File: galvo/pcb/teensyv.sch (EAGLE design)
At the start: 53 parts, among them IC1 RB-0512D, IC10 MCP4922-E/P, IC2.5 MAX6102, IC3 QUAD_OPAMPP, IC5 MAX6105, IC9 QUAD_OPAMPP

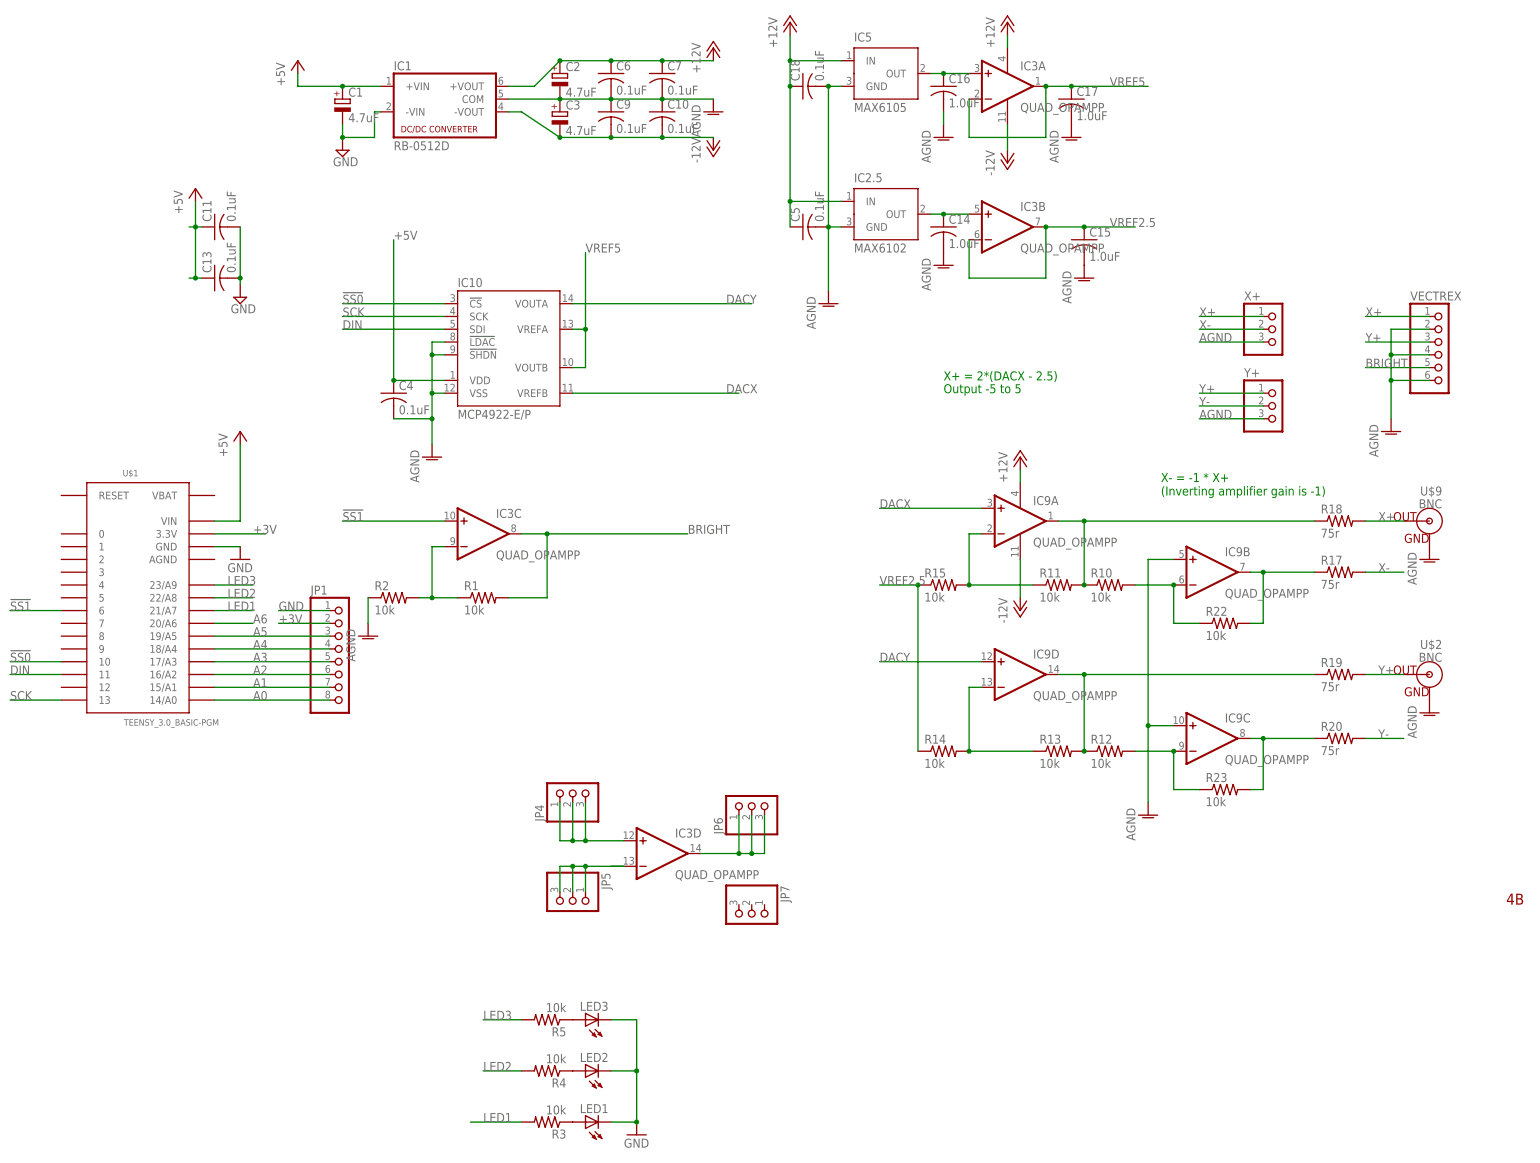
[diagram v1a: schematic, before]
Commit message: reworked board to have two DACs and proper differential amplifier
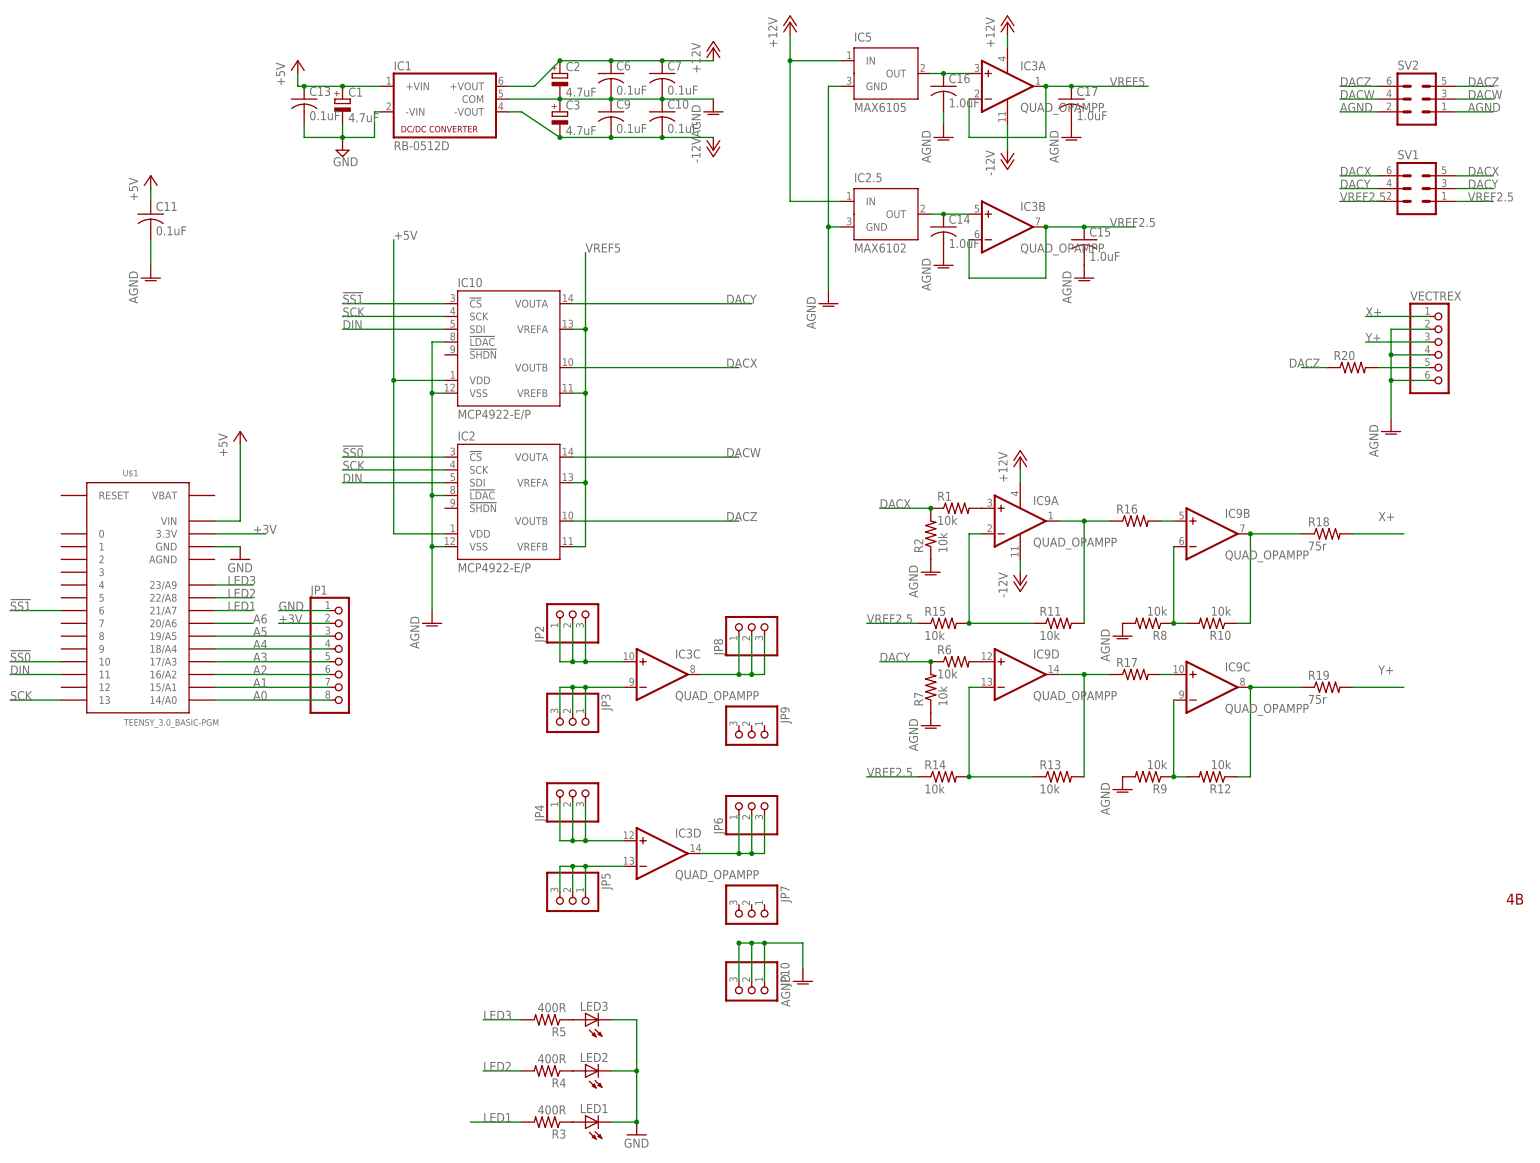
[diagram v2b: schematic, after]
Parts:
- removed C18, C4, C5: 0.1uF, adafruit:C-US025-024X044
- removed R22, R23: 10k, adafruit:R-US_0204/2V
- removed U$2, U$9: BNC, adafruit:BNC
- removed X+, Y+: (no value), adafruit:PINHD-1X3
- added IC2: MCP4922-E/P, nh-ic:MCP4922-E/P
- added JP10, JP2, JP3, JP8, JP9: (no value), adafruit:PINHD-1X3
- added R16: (no value), adafruit:R-US_0204/7
- added R6, R7, R8, R9: 10k, adafruit:R-US_0204/2V
- added SV1, SV2: (no value), con-lstb:MA03-2
- R17, R20: value 75r -> (none); device adafruit:R-US_0204/2V -> adafruit:R-US_0204/7
- R3, R4, R5: value 10k -> 400R
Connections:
- removed net BRIGHT: IC3C.OUT, R1.2, VECTREX.5
- removed net X-: R17.2, X+.2
- removed net Y-: R20.2, Y+.2
- new net DACW: IC2.VOUTA, SV2.3, SV2.4
- new net DACZ: IC2.VOUTB, R20.1, SV2.5, SV2.6
- new net N$14: IC9C.OUT, R12.1, R19.1
- new net N$16: IC9C.-IN, R12.2, R9.1
- new net N$17: IC9B.-IN, R10.2, R8.1
- new net N$20: IC3C.OUT, JP8.1, JP8.2, JP8.3
- new net N$21: IC9B.+IN, R16.2
- new net N$22: IC9C.+IN, R17.2
- new net N$23: R20.2, VECTREX.5
- net !SS0: now also IC2.!CS; no longer IC10.!CS
- net !SS1: now also IC10.!CS; no longer IC3C.+IN
- net +12V: no longer C18.1, C5.1
- net +5V: now also IC2.VDD; no longer C4.1
- net AGND: now also C11.2, IC2.!LDAC, IC2.VSS, JP10.1, JP10.2, JP10.3, R7.1, R8.2, R9.2, SV2.1, SV2.2; no longer C18.2, C4.2, C5.2, IC10.!SHDN, IC9B.+IN, IC9C.+IN, U$2.GND, U$9.GND, X+.3, Y+.3
- net DACX: now also IC10.VOUTB, R1.1, R2.2, SV1.5, SV1.6; no longer IC10.VREFB, IC9A.+IN
- net DACY: now also R6.1, R7.2, SV1.3, SV1.4; no longer IC9D.+IN
- net DIN: now also IC2.SDI
- net GND: no longer C11.2
- net N$13: now also R10.1, R18.1; no longer R17.1, R22.2
- net N$15: now also R17.1; no longer R12.1, R19.1
- net N$18: now also IC3C.-IN, JP3.1, JP3.2, JP3.3; no longer IC9C.OUT, R20.1, R23.2
- net N$19: now also IC3C.+IN, JP2.1, JP2.2, JP2.3; no longer IC9C.-IN, R12.2, R23.1
- net N$2: now also IC9A.+IN, R1.2; no longer IC3C.-IN, R1.1, R2.2
- net N$8: now also R16.1; no longer R10.1, R18.1
- net N$9: now also IC9D.+IN, R6.2; no longer IC9B.-IN, R10.2, R22.1
- net SCK: now also IC2.SCK
- net VREF2.5: now also SV1.1, SV1.2
- net VREF5: now also IC10.VREFB, IC2.VREFA, IC2.VREFB; no longer IC10.VOUTB
- net X+: no longer U$9.OUT, X+.1
- net Y+: no longer U$2.OUT, Y+.1
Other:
- note removed: "Output -5 to 5"
- note removed: "X+ = 2*(DACX - 2.5)"
- note removed: "X- = -1 * X+ (Inverting amplifier gain is -1)"
- moved on the sheet: C11, C13, IC3C, IC9B, IC9C, R1, R10, R11, R12, R13, R14, R15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

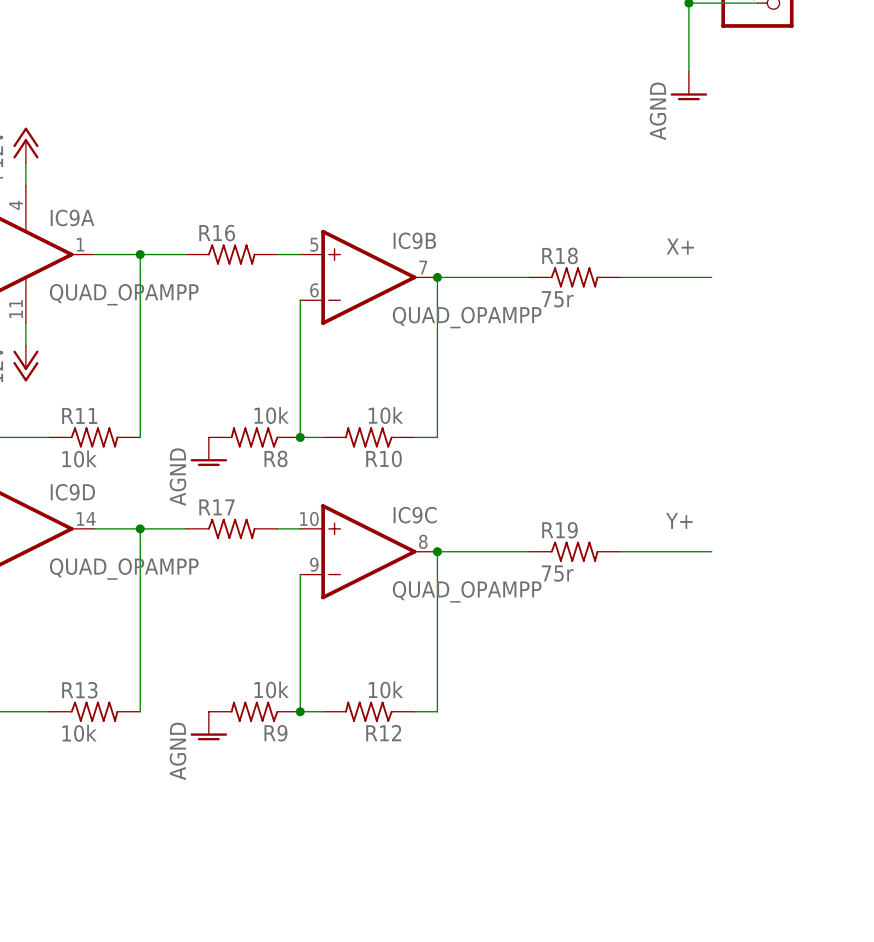
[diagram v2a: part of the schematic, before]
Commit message: convert to inverting opamp
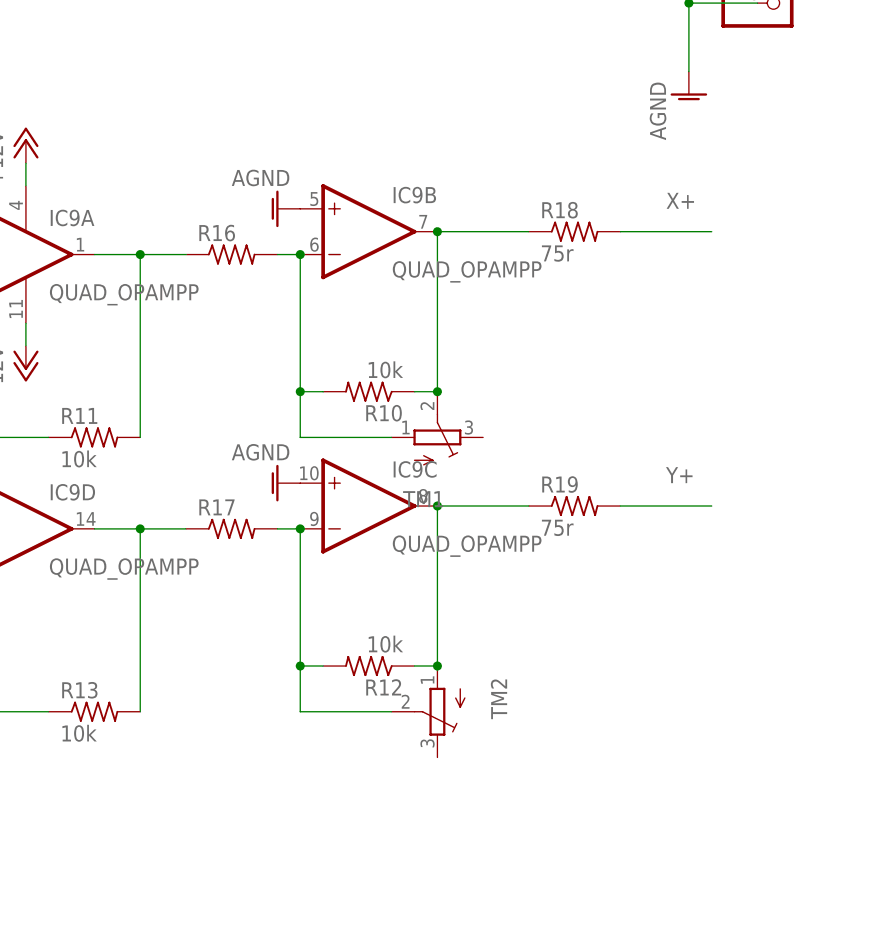
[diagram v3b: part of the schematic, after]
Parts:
- removed R8, R9: 10k, adafruit:R-US_0204/2V
- added TM1, TM2: (no value), adafruit:TRIMPOTTC33X
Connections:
- removed net N$21: IC9B.+IN, R16.2
- removed net N$22: IC9C.+IN, R17.2
- net AGND: now also IC9B.+IN, IC9C.+IN; no longer R8.2, R9.2
- net N$13: now also TM1.S
- net N$14: now also TM2.A
- net N$16: now also R17.2, TM2.S; no longer R9.1
- net N$17: now also R16.2, TM1.A; no longer R8.1
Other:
- moved on the sheet: IC9B, IC9C, R10, R12, R18, R19
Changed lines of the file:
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@@
 <part name="R10" library="adafruit" deviceset="R-US_" device="0204/2V" value="10k"/>
 <part name="R12" library="adafruit" deviceset="R-US_" device="0204/2V" value="10k"/>
-<part name="R8" library="adafruit" deviceset="R-US_" device="0204/2V" value="10k"/>
-<part name="R9" library="adafruit" deviceset="R-US_" device="0204/2V" value="10k"/>
 <part name="AGND3" library="supply1" deviceset="AGND" device=""/>
 <part name="AGND11" library="supply1" deviceset="AGND" device=""/>
@@
 <part name="AGND14" library="supply1" deviceset="AGND" device=""/>
 <part name="P+8" library="supply1" deviceset="+5V" device=""/>
+<part name="TM1" library="adafruit" deviceset="TRIMPOT" device="TC33X"/>
+<part name="TM2" library="adafruit" deviceset="TRIMPOT" device="TC33X"/>
 </parts>
 <sheets>
@@
 <instance part="IC10" gate="G$1" x="40.64" y="119.38"/>
 <instance part="IC9" gate="A" x="142.24" y="83.82"/>
-<instance part="IC9" gate="B" x="180.34" y="81.28"/>
+<instance part="IC9" gate="B" x="180.34" y="86.36"/>
 <instance part="R11" gate="G$1" x="149.86" y="63.5"/>
 <instance part="R13" gate="G$1" x="149.86" y="33.02"/>
 <instance part="R14" gate="G$1" x="127" y="33.02"/>
 <instance part="R15" gate="G$1" x="127" y="63.5"/>
-<instance part="R18" gate="G$1" x="203.2" y="81.28"/>
-<instance part="R19" gate="G$1" x="203.2" y="50.8"/>
+<instance part="R18" gate="G$1" x="203.2" y="86.36"/>
+<instance part="R19" gate="G$1" x="203.2" y="55.88"/>
 <instance part="IC9" gate="P" x="142.24" y="83.82"/>
 <instance part="P+6" gate="1" x="142.24" y="96.52"/>
@@
 <instance part="C15" gate="G$1" x="154.94" y="139.7"/>
 <instance part="IC9" gate="D" x="142.24" y="53.34"/>
-<instance part="IC9" gate="C" x="180.34" y="50.8"/>
+<instance part="IC9" gate="C" x="180.34" y="55.88"/>
 <instance part="AGND12" gate="VR1" x="25.4" y="63.5"/>
 <instance part="JP4" gate="A" x="53.34" y="30.48" rot="R90"/>
@@
 <instance part="AGND1" gate="VR1" x="124.46" y="73.66"/>
 <instance part="AGND2" gate="VR1" x="124.46" y="43.18"/>
-<instance part="R10" gate="G$1" x="180.34" y="63.5" rot="R180"/>
-<instance part="R12" gate="G$1" x="180.34" y="33.02" rot="R180"/>
-<instance part="R8" gate="G$1" x="167.64" y="63.5" rot="R180"/>
-<instance part="R9" gate="G$1" x="167.64" y="33.02" rot="R180"/>
-<instance part="AGND3" gate="VR1" x="162.56" y="60.96"/>
-<instance part="AGND11" gate="VR1" x="162.56" y="30.48"/>
+<instance part="R10" gate="G$1" x="180.34" y="68.58" rot="R180"/>
+<instance part="R12" gate="G$1" x="180.34" y="38.1" rot="R180"/>
+<instance part="AGND3" gate="VR1" x="170.18" y="88.9" rot="R270"/>
+<instance part="AGND11" gate="VR1" x="170.18" y="58.42" rot="R270"/>
 <instance part="JP2" gate="A" x="53.34" y="66.04" rot="R90"/>
 <instance part="JP3" gate="A" x="53.34" y="43.18" rot="R270"/>
@@
 <instance part="AGND14" gate="VR1" x="-30.48" y="132.08"/>
 <instance part="P+8" gate="1" x="-30.48" y="152.4"/>
+<instance part="TM1" gate="G$1" x="187.96" y="63.5" rot="MR90"/>
+<instance part="TM2" gate="G$1" x="187.96" y="33.02" rot="R180"/>
 </instances>
 <busses>
@@
 <segment>
 <pinref part="R18" gate="G$1" pin="2"/>
-<wire x1="208.28" y1="81.28" x2="218.44" y2="81.28" width="0.1524" layer="91"/>
-<label x="213.36" y="83.82" size="1.778" layer="95"/>
+<wire x1="208.28" y1="86.36" x2="218.44" y2="86.36" width="0.1524" layer="91"/>
+<label x="213.36" y="88.9" size="1.778" layer="95"/>
 </segment>
 <segment>
@@
 <segment>
 <pinref part="R19" gate="G$1" pin="2"/>
-<wire x1="208.28" y1="50.8" x2="218.44" y2="50.8" width="0.1524" layer="91"/>
-<label x="213.36" y="53.34" size="1.778" layer="95"/>
+<wire x1="208.28" y1="55.88" x2="218.44" y2="55.88" width="0.1524" layer="91"/>
+<label x="213.36" y="58.42" size="1.778" layer="95"/>
 </segment>
 <segment>
@@
 </segment>
 <segment>
-<pinref part="R8" gate="G$1" pin="2"/>
-<pinref part="AGND3" gate="VR1" pin="AGND"/>
-</segment>
-<segment>
-<pinref part="R9" gate="G$1" pin="2"/>
-<pinref part="AGND11" gate="VR1" pin="AGND"/>
-</segment>
-<segment>
 <pinref part="SV2" gate="1" pin="2"/>
 <wire x1="213.36" y1="165.1" x2="205.74" y2="165.1" width="0.1524" layer="91"/>
@@
 <wire x1="-30.48" y1="139.7" x2="-30.48" y2="134.62" width="0.1524" layer="91"/>
 </segment>
+<segment>
+<pinref part="IC9" gate="B" pin="+IN"/>
+<pinref part="AGND3" gate="VR1" pin="AGND"/>
+</segment>
+<segment>
+<pinref part="IC9" gate="C" pin="+IN"/>
+<pinref part="AGND11" gate="VR1" pin="AGND"/>
+</segment>
 </net>
 <net name="N$3" class="0">
@@
 <pinref part="IC9" gate="B" pin="OUT"/>
 <pinref part="R18" gate="G$1" pin="1"/>
-<wire x1="198.12" y1="81.28" x2="187.96" y2="81.28" width="0.1524" layer="91"/>
+<wire x1="198.12" y1="86.36" x2="187.96" y2="86.36" width="0.1524" layer="91"/>
 <pinref part="R10" gate="G$1" pin="1"/>
-<wire x1="185.42" y1="63.5" x2="187.96" y2="63.5" width="0.1524" layer="91"/>
-<wire x1="187.96" y1="63.5" x2="187.96" y2="81.28" width="0.1524" layer="91"/>
-<junction x="187.96" y="81.28"/>
+<wire x1="185.42" y1="68.58" x2="187.96" y2="68.58" width="0.1524" layer="91"/>
+<wire x1="187.96" y1="68.58" x2="187.96" y2="86.36" width="0.1524" layer="91"/>
+<junction x="187.96" y="86.36"/>
+<pinref part="TM1" gate="G$1" pin="S"/>
+<junction x="187.96" y="68.58"/>
 </segment>
 </net>
@@
 <pinref part="IC9" gate="C" pin="OUT"/>
 <pinref part="R19" gate="G$1" pin="1"/>
-<wire x1="198.12" y1="50.8" x2="187.96" y2="50.8" width="0.1524" layer="91"/>
+<wire x1="198.12" y1="55.88" x2="187.96" y2="55.88" width="0.1524" layer="91"/>
 <pinref part="R12" gate="G$1" pin="1"/>
-<wire x1="185.42" y1="33.02" x2="187.96" y2="33.02" width="0.1524" layer="91"/>
-<wire x1="187.96" y1="33.02" x2="187.96" y2="50.8" width="0.1524" layer="91"/>
-<junction x="187.96" y="50.8"/>
+<wire x1="185.42" y1="38.1" x2="187.96" y2="38.1" width="0.1524" layer="91"/>
+<wire x1="187.96" y1="38.1" x2="187.96" y2="55.88" width="0.1524" layer="91"/>
+<junction x="187.96" y="55.88"/>
+<pinref part="TM2" gate="G$1" pin="A"/>
+<junction x="187.96" y="38.1"/>
 </segment>
 </net>
@@
 <segment>
 <pinref part="IC9" gate="C" pin="-IN"/>
-<wire x1="172.72" y1="48.26" x2="172.72" y2="33.02" width="0.1524" layer="91"/>
+<wire x1="172.72" y1="53.34" x2="172.72" y2="38.1" width="0.1524" layer="91"/>
 <pinref part="R12" gate="G$1" pin="2"/>
-<wire x1="172.72" y1="33.02" x2="175.26" y2="33.02" width="0.1524" layer="91"/>
-<junction x="172.72" y="33.02"/>
-<pinref part="R9" gate="G$1" pin="1"/>
+<wire x1="172.72" y1="38.1" x2="175.26" y2="38.1" width="0.1524" layer="91"/>
+<pinref part="R17" gate="G$1" pin="2"/>
+<wire x1="172.72" y1="53.34" x2="170.18" y2="53.34" width="0.1524" layer="91"/>
+<junction x="172.72" y="53.34"/>
+<wire x1="182.88" y1="33.02" x2="172.72" y2="33.02" width="0.1524" layer="91"/>
+<wire x1="172.72" y1="33.02" x2="172.72" y2="38.1" width="0.1524" layer="91"/>
+<junction x="172.72" y="38.1"/>
+<pinref part="TM2" gate="G$1" pin="S"/>
 </segment>
 </net>
 <net name="N$17" class="0">
 <segment>
-<pinref part="R8" gate="G$1" pin="1"/>
 <pinref part="R10" gate="G$1" pin="2"/>
-<wire x1="172.72" y1="63.5" x2="175.26" y2="63.5" width="0.1524" layer="91"/>
+<wire x1="172.72" y1="68.58" x2="175.26" y2="68.58" width="0.1524" layer="91"/>
 <pinref part="IC9" gate="B" pin="-IN"/>
-<wire x1="172.72" y1="78.74" x2="172.72" y2="63.5" width="0.1524" layer="91"/>
-<junction x="172.72" y="63.5"/>
+<wire x1="172.72" y1="83.82" x2="172.72" y2="68.58" width="0.1524" layer="91"/>
+<pinref part="R16" gate="G$1" pin="2"/>
+<wire x1="172.72" y1="83.82" x2="170.18" y2="83.82" width="0.1524" layer="91"/>
+<junction x="172.72" y="83.82"/>
+<wire x1="182.88" y1="63.5" x2="172.72" y2="63.5" width="0.1524" layer="91"/>
+<wire x1="172.72" y1="63.5" x2="172.72" y2="68.58" width="0.1524" layer="91"/>
+<junction x="172.72" y="68.58"/>
+<pinref part="TM1" gate="G$1" pin="A"/>
 </segment>
 </net>
@@
 </segment>
 </net>
-<net name="N$21" class="0">
-<segment>
-<pinref part="IC9" gate="B" pin="+IN"/>
-<pinref part="R16" gate="G$1" pin="2"/>
-<wire x1="170.18" y1="83.82" x2="172.72" y2="83.82" width="0.1524" layer="91"/>
-</segment>
-</net>
-<net name="N$22" class="0">
-<segment>
-<pinref part="IC9" gate="C" pin="+IN"/>
-<pinref part="R17" gate="G$1" pin="2"/>
-<wire x1="170.18" y1="53.34" x2="172.72" y2="53.34" width="0.1524" layer="91"/>
-</segment>
-</net>
